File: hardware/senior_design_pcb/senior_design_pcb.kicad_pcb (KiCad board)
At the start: 4 copper layers, 67.2 x 67.2 mm, 89 parts, among them J1 SBH11-PBPC-D05-ST-BK, J10 Conn_01x04_Socket, J11 2x08Rectangle-LED Matrix Conn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, J12 1x05JST - Joystick2 connector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, J13 UJ20-C-H-C-4-SMT-TR, J2 Conn_01x08_Pin, J3 Conn_01x02_Socket, J4 Conn_01x02_Socket, J5 1x05JST-Admin LCD Console Con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, J6 1x05JST - Joystick1 connector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, J9 Conn_01x04_Socket, SW3 1x02JST-Admin Console button 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, U1 KMR241GLFS, U10 KMR241GLFS, U2 STM32F091RCTx, U3 LD1117S33TR_SOT223, U4 KMR241GLFS, U5 USBLC6-2SC6Y, U6 2SA1873-GRTE85L_F, U7 2SA1873-GRTE85L_F, U8 2SA1873-GRTE85L_F, U9 KMR241GLFS

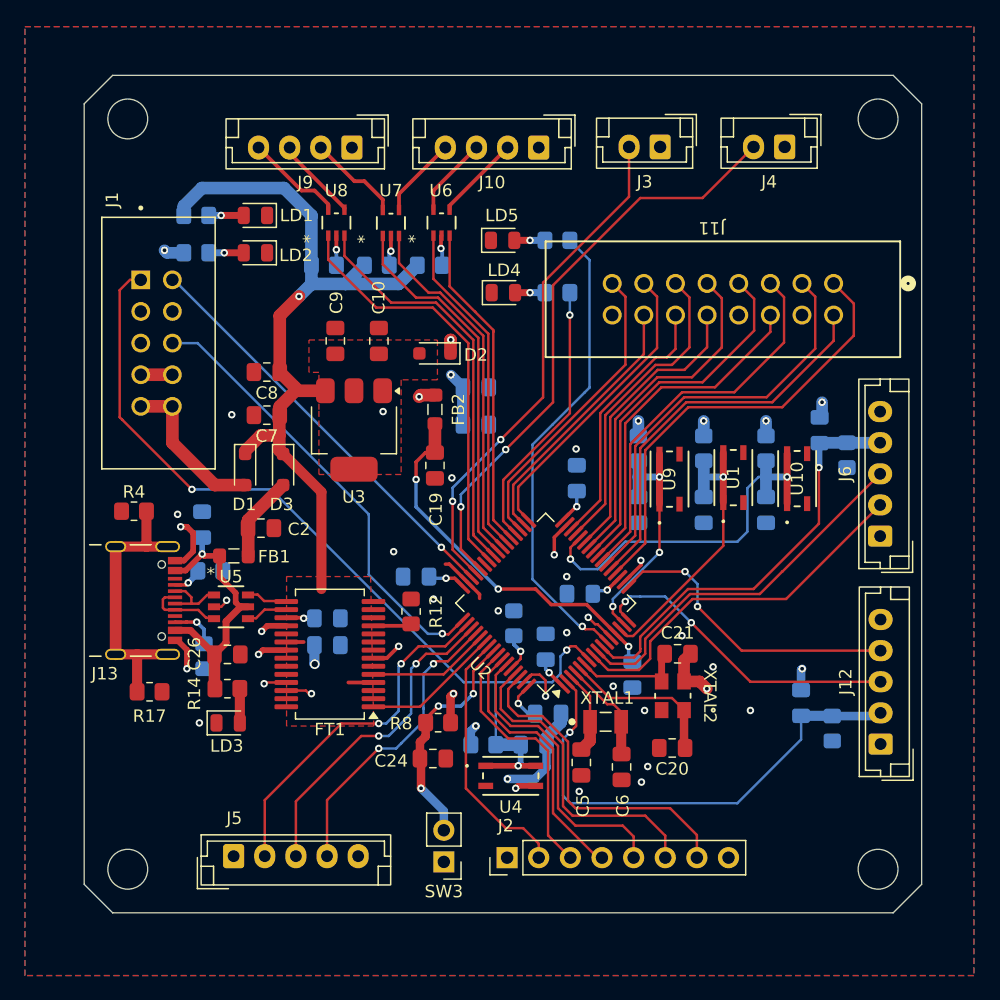
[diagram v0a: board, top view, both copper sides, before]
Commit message: 3v3 exclusion zones
decoupling caps had connection to 3v3 straight to the pin. should route through the cap not just be attached. adding exclusion zones to vias and routing 3v3 to the cap pad
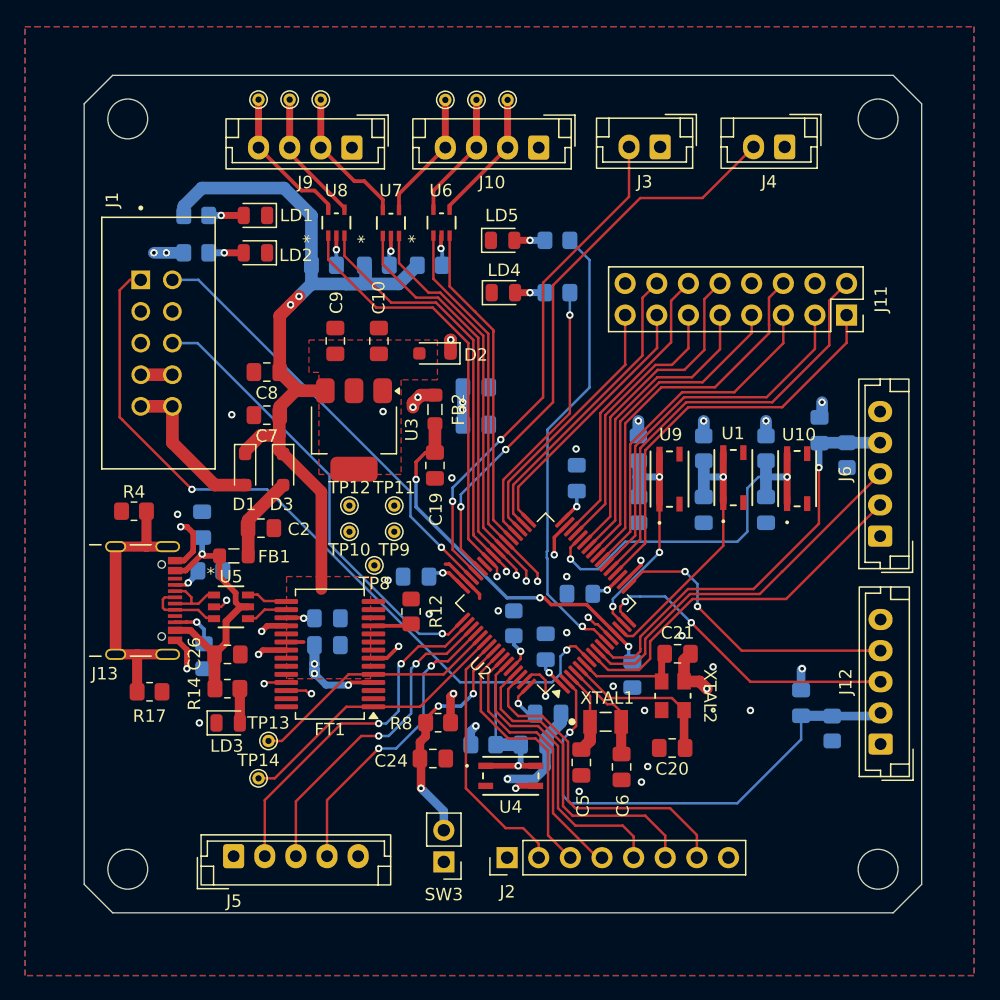
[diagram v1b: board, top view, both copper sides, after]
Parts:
- added TP1: TestPoint_Small, TestPoint:TestPoint_THTPad_D1.0mm_Drill0.5mm, F.Cu at (49.0, 21.1)
- added TP10: TestPoint_Small, TestPoint:TestPoint_THTPad_D1.0mm_Drill0.5mm, F.Cu at (41.3, 55.8)
- added TP11: TestPoint_Small, TestPoint:TestPoint_THTPad_D1.0mm_Drill0.5mm, F.Cu at (44.9, 53.7)
- added TP12: TestPoint_Small, TestPoint:TestPoint_THTPad_D1.0mm_Drill0.5mm, F.Cu at (41.3, 53.7)
- added TP13: TestPoint_Small, TestPoint:TestPoint_THTPad_D1.0mm_Drill0.5mm, F.Cu at (34.8, 72.6)
- added TP14: TestPoint_Small, TestPoint:TestPoint_THTPad_D1.0mm_Drill0.5mm, F.Cu at (34.0, 75.6)
- added TP2: TestPoint_Small, TestPoint:TestPoint_THTPad_D1.0mm_Drill0.5mm, F.Cu at (51.5, 21.1)
- added TP3: TestPoint_Small, TestPoint:TestPoint_THTPad_D1.0mm_Drill0.5mm, F.Cu at (54.0, 21.1)
- added TP4: TestPoint_Small, TestPoint:TestPoint_THTPad_D1.0mm_Drill0.5mm, F.Cu at (34.0, 21.1)
- added TP5: TestPoint_Small, TestPoint:TestPoint_THTPad_D1.0mm_Drill0.5mm, F.Cu at (36.5, 21.1)
- added TP6: TestPoint_Small, TestPoint:TestPoint_THTPad_D1.0mm_Drill0.5mm, F.Cu at (39.0, 21.1)
- added TP8: TestPoint_Small, TestPoint:TestPoint_THTPad_D1.0mm_Drill0.5mm, F.Cu at (43.3, 58.5)
- added TP9: TestPoint_Small, TestPoint:TestPoint_THTPad_D1.0mm_Drill0.5mm, F.Cu at (44.9, 55.8)
- J11: footprint kicad_library:jst-02x08 conn -> Connector_PinSocket_2.54mm:PinSocket_2x08_P2.54mm_Vertical
- moved J11 2.74 mm to (81.2, 38.4), turned to -90 degrees
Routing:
- net /PC8: track 28.9 -> 49.4 mm, vias 0 -> 1
- net /PC7: track 27.1 -> 47.0 mm, vias 0 -> 1
- net /PA8: track 32.7 -> 51.2 mm, vias 0 -> 1
- net /PC9: track 30.2 -> 46.5 mm, vias 0 -> 1
- net /PA9: track 34.0 -> 48.4 mm, vias 0 -> 1
- net /PD2: track 11.1 -> 22.7 mm
- net /PC12: track 9.80 -> 20.4 mm
- net +5V: track 68.2 -> 73.2 mm, vias 2 -> 5
- net /PUL+1: track 7.92 -> 11.8 mm
- net /ENA+1: track 7.55 -> 11.4 mm
- net /DIR+1: track 6.81 -> 10.7 mm
- net /ENA+2: track 6.92 -> 10.7 mm
- net /DIR+2: track 6.42 -> 10.2 mm
- net /PUL+2: track 6.56 -> 10.4 mm
- net /PA4: track 36.3 -> 32.8 mm
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
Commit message: updated pcb
changes:
-all suggested from Setsuna & Shivam & presentation feedback
	-removed r4 and r17
	-kept multiple net names (following PCB Design Techniques - Spring 2025 from brightspace)
	-fixed XTAL1 missing connection
	-removed PWR_FLAG on GND
	-removed D2 - no need
	-increased via hole size (15 mil drill + 28 mil diameter)
	-kept chamfer (compared prices on jlc and pcbway and same price)
	-removed via on SW3
	-did not change traces beneath oscillators, everythings already routed but will keep in mind for the future
	-moved silkscreen names from off the board to on the board (we are still discussing decorative designs - if we include any)
	-kept FB since FB should be near source of noise and source of noise we are trying to prevent is from the USB-C. if we are misunderstanding this please let us know.
	-trace clearances updated, needed more with via size increase
	-moved silkscren + labeled pins
	-removed 3v connection from stlink. keeping only 5v

	-also, the led matrix connector somehow relapsed and changed to the 2x08 default header instead of a jtag type rectangular connector. updated and fixed :)

From prof. walters feedback:
-added back shield resistor
-added tvs diodes for joystick + buttons
-changed decoupling cap value
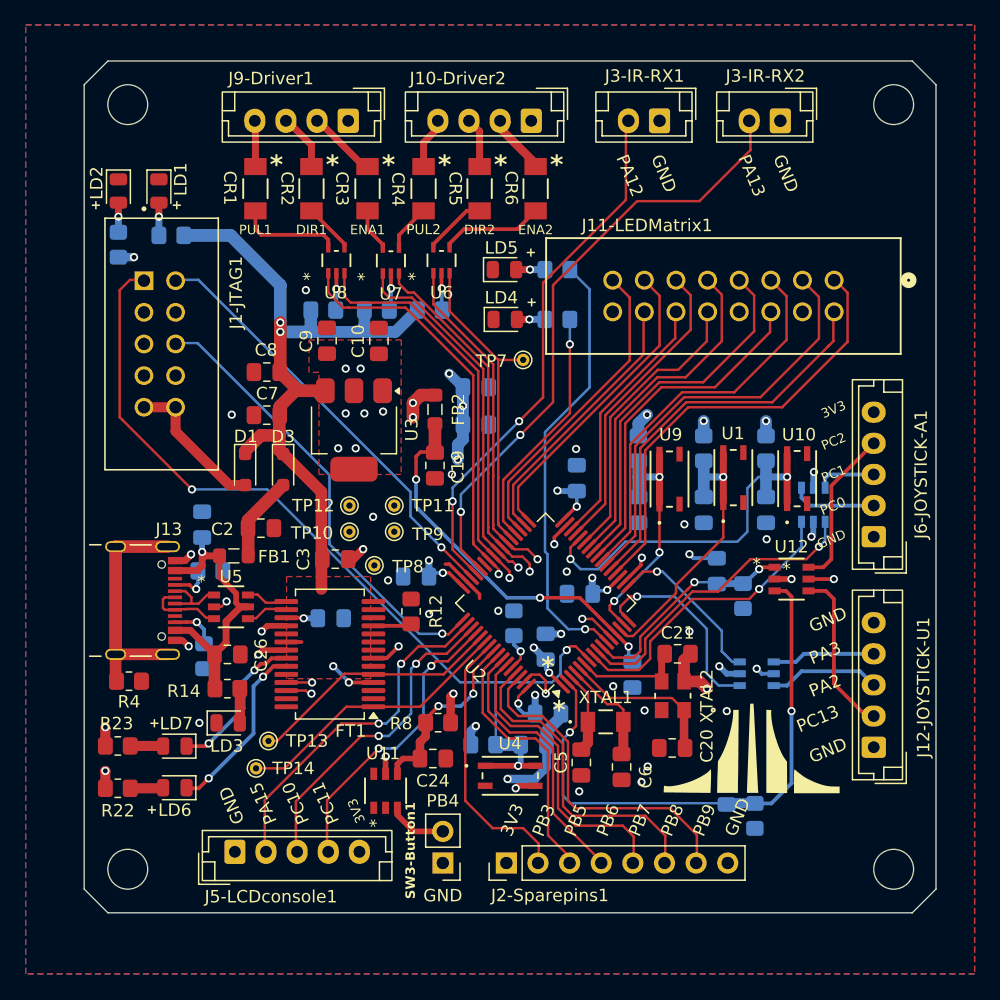
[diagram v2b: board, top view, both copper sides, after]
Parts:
- removed D2: BAT60JFILM, Diode_SMD:D_SOD-323_HandSoldering
- removed J1: SBH11-PBPC-D05-ST-BK, Sr_ Design:jtag_conn
- removed J10, J9: Conn_01x04_Socket, Connector_JST:JST_EH_B4B-EH-A_1x04_P2.50mm_Vertical
- removed J11: 2x08Rectangle-LED Matrix Connector, Connector_PinSocket_2.54mm:PinSocket_2x08_P2.54mm_Vertical
- removed J12: 1x05JST - Joystick2 connector (gamer), Connector_JST:JST_EH_B5B-EH-A_1x05_P2.50mm_Vertical
- removed J2: Conn_01x08_Pin, Connector_PinHeader_2.54mm:PinHeader_1x08_P2.54mm_Vertical
- removed J3, J4: Conn_01x02_Socket, Connector_JST:JST_EH_B2B-EH-A_1x02_P2.50mm_Vertical
- removed J5: 1x05JST-Admin LCD Console Connector, Connector_JST:JST_EH_B5B-EH-A_1x05_P2.50mm_Vertical
- removed J6: 1x05JST - Joystick1 connector (admin), Connector_JST:JST_EH_B5B-EH-A_1x05_P2.50mm_Vertical
- removed R17: 1M, Resistor_SMD:R_0805_2012Metric_Pad1.20x1.40mm_HandSolder
- removed SW3: 1x02JST-Admin Console button connector, Connector_PinHeader_2.54mm:PinHeader_1x02_P2.54mm_Vertical
- removed TP1, TP2, TP3, TP4, TP5, TP6: TestPoint_Small, TestPoint:TestPoint_THTPad_D1.0mm_Drill0.5mm
- added CR1: JAN1N4148UR-1, kicad_library:jan1n4148 smd diode-M, F.Cu at (33.8, 28.2)
- added CR2: JAN1N4148UR-1, kicad_library:jan1n4148 smd diode-M, F.Cu at (38.2, 28.2)
- added CR3: JAN1N4148UR-1, kicad_library:jan1n4148 smd diode-M, F.Cu at (42.7, 28.2)
- added CR4: JAN1N4148UR-1, kicad_library:jan1n4148 smd diode-M, F.Cu at (47.2, 28.2)
- added CR5: JAN1N4148UR-1, kicad_library:jan1n4148 smd diode-M, F.Cu at (51.7, 28.2)
- added CR6: JAN1N4148UR-1, kicad_library:jan1n4148 smd diode-M, F.Cu at (56.2, 28.2)
- added G***: LOGO, LOGO, F.Cu at (73.5, 72.7)
- added J1-JTAG1: SBH11-PBPC-D05-ST-BK, Sr_ Design:jtag_conn, F.Cu at (26.1, 40.7)
- added J10-Driver2: Conn_01x04_Socket, Connector_JST:JST_EH_B4B-EH-A_1x04_P2.50mm_Vertical, F.Cu at (55.9, 22.8)
- added J11-LEDMatrix1: 2x08Rectangle-LED Matrix Connector, General Library:jst-02x08 conn, F.Cu at (80.2, 35.6)
- added J12-JOYSTICK-U1: 1x05JST - Joystick2 connector (gamer), Connector_JST:JST_EH_B5B-EH-A_1x05_P2.50mm_Vertical, F.Cu at (83.4, 73.1)
- added J2-Sparepins1: Conn_01x08_Pin, Connector_PinHeader_2.54mm:PinHeader_1x08_P2.54mm_Vertical, F.Cu at (53.9, 82.4)
- added J3-IR-RX1: Conn_01x02_Socket, Connector_JST:JST_EH_B2B-EH-A_1x02_P2.50mm_Vertical, F.Cu at (66.2, 22.8)
- added J3-IR-RX2: Conn_01x02_Socket, Connector_JST:JST_EH_B2B-EH-A_1x02_P2.50mm_Vertical, F.Cu at (75.9, 22.8)
- added J5-LCDconsole1: 1x05JST-Admin LCD Console Connector, Connector_JST:JST_EH_B5B-EH-A_1x05_P2.50mm_Vertical, F.Cu at (32.1, 81.5)
- added J6-JOYSTICK-A1: 1x05JST - Joystick1 connector (admin), Connector_JST:JST_EH_B5B-EH-A_1x05_P2.50mm_Vertical, F.Cu at (83.4, 56.2)
- added J9-Driver1: Conn_01x04_Socket, Connector_JST:JST_EH_B4B-EH-A_1x04_P2.50mm_Vertical, F.Cu at (41.2, 22.8)
- added LD6: LED_Red, LED_SMD:LED_0805_2012Metric, F.Cu at (27.3, 76.4)
- added LD7: LED_Green, LED_SMD:LED_0805_2012Metric, F.Cu at (27.3, 73.0)
- added R22: 150, Resistor_SMD:R_0805_2012Metric_Pad1.20x1.40mm_HandSolder, F.Cu at (22.7, 76.4)
- added R23: 150, Resistor_SMD:R_0805_2012Metric_Pad1.20x1.40mm_HandSolder, F.Cu at (22.7, 73.0)
- added SW3-Button1: 1x02JST-Admin Console button connector, Connector_PinHeader_2.54mm:PinHeader_1x02_P2.54mm_Vertical, F.Cu at (48.8, 82.4)
- added TP7: TestPoint_Small, TestPoint:TestPoint_THTPad_D1.0mm_Drill0.5mm, F.Cu at (55.2, 42.0)
- added U11: USBLC6-2SC6Y, Sr_ Design:TVS-DIODE-USBLC6-2SC6Y, F.Cu at (44.2, 76.6)
- added U12: USBLC6-2SC6Y, Sr_ Design:TVS-DIODE-USBLC6-2SC6Y, F.Cu at (76.8, 59.6)
- added U13: USBLC6-2SC6Y, Sr_ Design:TVS-DIODE-USBLC6-2SC6Y, B.Cu at (74.0, 67.2)
- added U14: USBLC6-2SC6Y, Sr_ Design:TVS-DIODE-USBLC6-2SC6Y, B.Cu at (78.5, 53.6)
- C17: value 1uf -> .1uf
- C3: moved to F.Cu
- C5, C6: value 20pF -> 7pF
- R14: value 5k11 -> 150
- R4: value 1M -> 100M
- XTAL1: footprint kicad_library:32KHZ-CLK-ECX1293 -> kicad_library:32khz clock - crystal
- moved R9 14.1 mm to (72.9, 61.0)
- moved C23 14.0 mm to (70.8, 59.0)
- moved R4 13.7 mm to (23.6, 67.8)
- moved LD2 12.1 mm to (22.8, 28.4), turned to -90 degrees
- moved R10 9.37 mm to (73.9, 78.6)
- moved C25 9.29 mm to (71.6, 76.7)
- moved LD1 7.99 mm to (26.0, 28.4), turned to -90 degrees
- moved C3 6.94 mm to (40.2, 58.0)
- moved R5 6.28 mm to (22.8, 32.8), turned to 90 degrees
- moved R13 3.60 mm to (39.2, 38.0)
- moved R11 3.60 mm to (47.8, 38.0)
- moved R15 3.60 mm to (43.5, 38.0)
- moved U6 3.02 mm to (48.7, 34.0)
- moved U8 3.02 mm to (40.3, 34.0)
- moved U7 3.02 mm to (44.6, 34.0)
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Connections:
- C10 pad 1: /3v3-vo -> +3V3
- C9 pad 1: /3v3-vo -> +3V3
- FT1 pad 22: unconnected-(FT1-CBUS1-Pad22) -> Net-(FT1-CBUS1)
- FT1 pad 23: unconnected-(FT1-CBUS0-Pad23) -> Net-(FT1-CBUS0)
- J13 pad SH1: /usbc-shield -> Net-(J13-SHIELD)
- J13 pad SH2: /usbc-shield -> Net-(J13-SHIELD)
- J13 pad SH3: /usbc-shield -> Net-(J13-SHIELD)
- J13 pad SH4: /usbc-shield -> Net-(J13-SHIELD)
- R4 pad 1: /usbc-shield -> GND
- R4 pad 2: GND -> Net-(J13-SHIELD)
- U3 pad 2: /3v3-vo -> +3V3
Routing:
- net /usbc-shield: track 22.9 -> 0.00 mm
- net +3V3: track 34.8 -> 55.6 mm, vias 19 -> 35
- net Net-(J13-SHIELD): track 0.00 -> 19.2 mm
- net /ADMIN_JOYSTICK-BUTTON: track 34.1 -> 18.3 mm, vias 1 -> 2
- net Net-(FT1-CBUS0): track 0.00 -> 14.5 mm, vias 0 -> 2
- net Net-(J12-JOYSTICK-U1-Pin_2): track 0.00 -> 13.7 mm
- net Net-(J6-JOYSTICK-A1-Pin_4): track 0.00 -> 12.8 mm
- net Net-(FT1-CBUS1): track 0.00 -> 12.2 mm, vias 0 -> 2
- net /PA3: track 24.4 -> 13.4 mm, vias 2 -> 1
- net Net-(J12-JOYSTICK-U1-Pin_3): track 0.00 -> 8.97 mm
- net /PA2: track 25.4 -> 16.6 mm, vias 2 -> 1
- net Net-(J12-JOYSTICK-U1-Pin_4): track 0.00 -> 8.30 mm
- net /ENA+1: track 11.4 -> 3.47 mm
- net +5V: track 73.2 -> 65.4 mm, vias 5 -> 4
- net Net-(J6-JOYSTICK-A1-Pin_2): track 0.00 -> 7.07 mm
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- added copper zone on F.Cu, net +3V3
- removed copper zone on F.Cu, net /3v3-vo
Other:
- board size 67.2 x 67.2 mm -> 68.4 x 68.4 mm
- board text added: "*"
- board text added: "+"
- board text added: "3V3"
- board text added: "A PB0"
- board text added: "B PB1"
- board text added: "B1 PA6"
- board text added: "B2 PC5"
- board text added: "C PB10"
- board text added: "CLK PB12"
- board text added: "CONSOLE-DISP-1"
- board text added: "CONSOLE-DISP-2"
- board text added: "CONSOLE-DISP-3"
- board text added: "D PB11"
- board text added: "DIR1"
- board text added: "DIR2"
- board text added: "ENA1"
- board text added: "ENA2"
- board text added: "G1 PA5"
- board text added: "G2 PC4"
- board text added: "GND"
- board text added: "IR-IN-1"
- board text added: "IR-IN-2"
- board text added: "LAT PB13"
- board text added: "OE PB14"
- board text added: "PA12"
- board text added: "PA13"
- board text added: "PA15"
- board text added: "PA2"
- board text added: "PA3"
- board text added: "PB3"
- board text added: "PB4"
- board text added: "PB5"
- board text added: "PB6"
- board text added: "PB7"
- board text added: "PB8"
- board text added: "PB9"
- board text added: "PC0"
- board text added: "PC1"
- board text added: "PC10"
- board text added: "PC11"
- board text added: "PC13"
- board text added: "PC2"
- board text added: "PUL1"
- board text added: "PUL2"
- board text added: "R1 PA4"
- board text added: "R2 PA7"
- board text removed: "edge cuts is the whole area so that it stops throwing ground flywires. this is by no means the size we expect"
- board text removed: "the connectors are all 2.5 NOT 2.56mm rn"

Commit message: final gerber
ordered pcb
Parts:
- added G***: LOGO, LOGO, F.Cu at (56.7, 61.0)
- added G***: LOGO, LOGO, F.Cu at (23.3, 60.8)
- added G***: LOGO, LOGO, F.Cu at (59.1, 44.3)
- added G***: LOGO, LOGO, B.Cu at (37.8, 48.0)
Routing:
- net GND: track 51.7 -> 52.0 mm, vias 40 -> 41
